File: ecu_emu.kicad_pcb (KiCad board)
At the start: 2 copper layers, 51.3 x 16.5 mm, 29 parts, among them J1 Conn_02x06_Odd_Even, J2 Conn_01x04_Male, Q1 IRF7201PBF, U1 LD1117S33TR_SOT223, U2 STM32F105RBTx, U3 FAN73711, U4 E-L9637D, Y1 Crystal KX-9A

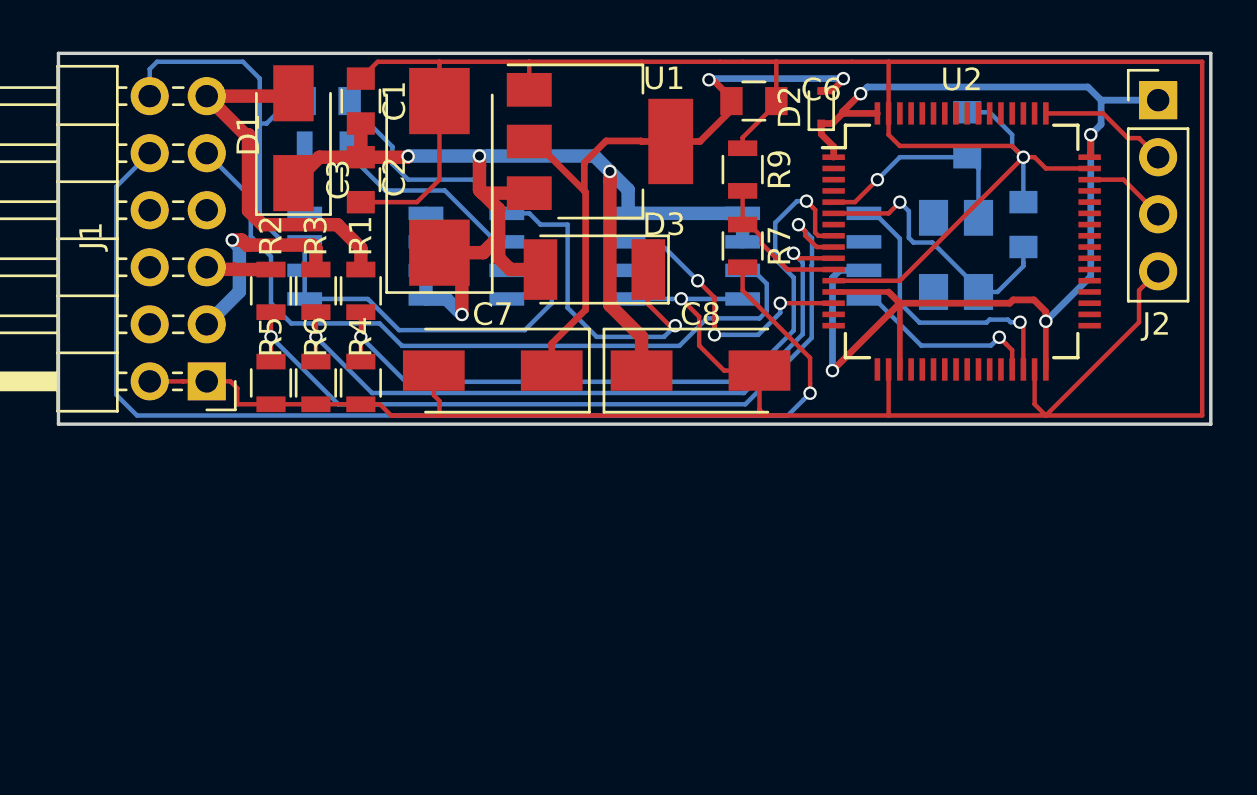
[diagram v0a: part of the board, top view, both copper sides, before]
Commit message: scheme: change solenoid driver, add capasitors to stm power supply, fix crystal package
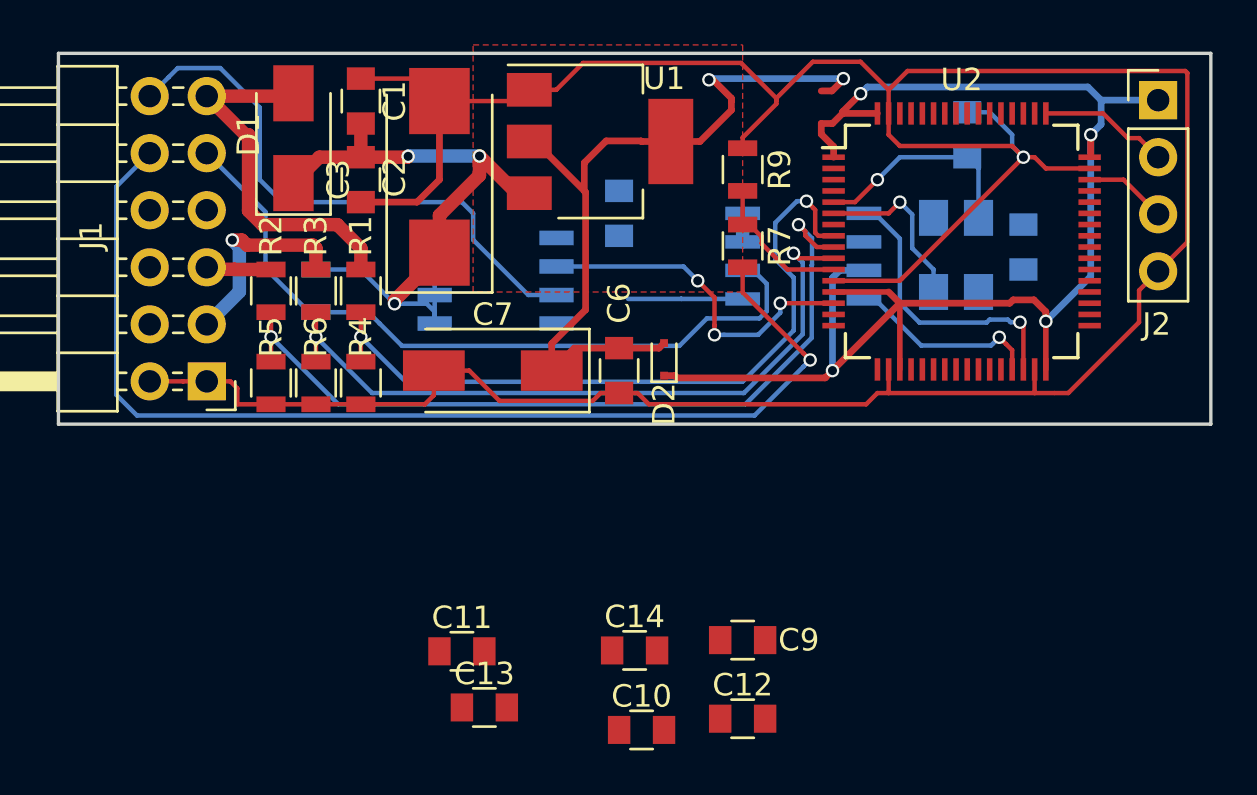
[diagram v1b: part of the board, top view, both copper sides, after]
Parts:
- removed D3: SM4007, Diodes_SMD:D_MELF
- removed Q1: IRF7201PBF, Housings_SOIC:SOIC-8_3.9x4.9mm_Pitch1.27mm
- added C10: 100nF, Capacitors_SMD:C_0805, F.Cu at (123.5, 109.5)
- added C11: 100nF, Capacitors_SMD:C_0805, F.Cu at (115.5, 106.0)
- added C12: 100nF, Capacitors_SMD:C_0805, F.Cu at (128.0, 109.0)
- added C13: 100nF, Capacitors_SMD:C_0805, F.Cu at (116.5, 108.5)
- added C14: 100nF, Capacitors_SMD:C_0805, F.Cu at (123.2, 106.0)
- C8: value 47uF x 16V -> 1nF; footprint Capacitors_Tantalum_SMD:CP_Tantalum_Case-C_EIA-6032-28_Wave -> Capacitors_SMD:C_0805; moved to B.Cu
- C9: value 1000 pF -> 4.7uF; moved to F.Cu
- R8: value 65 -> 1k
- U3: value FAN73711 -> BSP742R; footprint Housings_SOIC:SOIC-8_3.9x4.9mm_Pitch1.27mm -> zulljon:SOIC127P600X175-8N
- moved C9 30.3 mm to (128.0, 105.5)
- moved C6 13.4 mm to (122.5, 93.5), turned to 270 degrees
- moved D2 13.2 mm to (124.5, 93.0)
- moved C8 7.88 mm to (122.5, 86.5), turned to 90 degrees
- moved R8 6.47 mm to (109.0, 90.0), turned to 90 degrees
- moved U3 3.38 mm to (117.0, 89.5)
- moved C5 1.00 mm to (140.5, 88.0)
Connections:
- net /stm2K-BUS_UART_RX renamed /stm2Kbus_UART_RX
- net /stm2K-BUS_UART_TX renamed /stm2Kbus_UART_TX
- C1 pad 1: /K-BUS_Vbatt -> /Kbus_Vbatt
- C2 pad 1: /K-BUS_Vbatt -> /Kbus_Vbatt
- C3 pad 1: /K-BUS_Vbatt -> /Kbus_Vbatt
- C8 pad 1: /K-BUS_Vbatt -> /ECU_Kbus
- C9 pad 1: Net-(C9-Pad1) -> /+3V3_STM
- C9 pad 2: /ECU_solenoid -> GND
- D1 pad 1: /K-BUS_Vbatt -> /Kbus_Vbatt
- J1 pad 9: /ECU_K-BUS -> /ECU_Kbus
- R8 pad 1: Net-(Q1-Pad4) -> /ECU_Kbus
- R8 pad 2: Net-(R8-Pad2) -> /Kbus_Vbatt
- U1 pad 3: /K-BUS_Vbatt -> /Kbus_Vbatt
- U3 pad 1: /K-BUS_Vbatt -> GND
- U3 pad 3: (no net) -> /ECU_solenoid
- U3 pad 4: GND -> (no net)
- U3 pad 5: (no net) -> /Kbus_Vbatt
- U3 pad 6: /ECU_solenoid -> /Kbus_Vbatt
- U3 pad 7: Net-(R8-Pad2) -> /Kbus_Vbatt
- U3 pad 8: Net-(C9-Pad1) -> /Kbus_Vbatt
- U4 pad 6: /ECU_K-BUS -> /ECU_Kbus
- U4 pad 7: /K-BUS_Vbatt -> /Kbus_Vbatt
- U4 pad 8: /K-BUS_Vbatt -> /Kbus_Vbatt
- Y1 pad 2: Net-(C5-Pad1) -> GND
- Y1 pad 3: (no net) -> Net-(C5-Pad1)
- Y1 pad 4: (no net) -> GND
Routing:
- net /K-BUS_Vbatt: track 55.3 -> 0.00 mm, vias 4 -> 0
- net /ECU_K-BUS: track 33.9 -> 0.00 mm
- net /ECU_Kbus: track 0.00 -> 33.6 mm
- net /Kbus_Vbatt: track 0.00 -> 33.0 mm, vias 0 -> 3
- net GND: track 173.2 -> 144.2 mm, vias 2 -> 1
- net Net-(C9-Pad1): track 24.9 -> 0.00 mm, vias 1 -> 0
- net /ECU_solenoid: track 35.1 -> 25.4 mm
- net Net-(R8-Pad2): track 9.04 -> 0.00 mm
- net /+3V3_STM: track 56.5 -> 64.2 mm
- net /+3V3: track 29.9 -> 35.4 mm
- net Net-(C5-Pad1): track 12.4 -> 7.78 mm
- net Net-(Q1-Pad4): track 3.00 -> 0.00 mm
- net /solenoid_driver: track 12.7 -> 15.4 mm
- net /ECU_HALL_sensor+: track 49.9 -> 49.0 mm
- added copper zone on F.Cu, net /+3V3

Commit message: pcb: swd conn to socket strip, applied sch changes from 059fb19
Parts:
- C10, C11, C12, C13, C14, C9, R7, R9: moved to B.Cu
- J2: footprint Pin_Headers:Pin_Header_Straight_1x04_Pitch2.54mm -> Socket_Strips:Socket_Strip_Angled_1x04_Pitch2.54mm
- U3: footprint zulljon:SOIC127P600X175-8N -> Housings_SOIC:SOIC-8_3.9x4.9mm_Pitch1.27mm
- moved C13 36.1 mm to (140.5, 81.5), turned to 180 degrees
- moved C11 28.9 mm to (140.5, 91.5), turned to 180 degrees
- moved C10 27.8 mm to (140.5, 87.5), turned to 180 degrees
- moved C12 26.6 mm to (140.5, 85.5), turned to 180 degrees
- moved C9 25.3 mm to (140.5, 83.5)
- moved C14 23.9 mm to (140.5, 89.5), turned to 180 degrees
- moved C8 13.5 mm to (109.0, 86.0), turned to 270 degrees
- moved J2 9.98 mm to (146.5, 91.4), turned to 180 degrees
- moved U4 6.18 mm to (124.6, 89.5)
- moved R7 6.03 mm to (129.0, 82.0)
- moved C5 4.74 mm to (136.0, 89.5), turned to 0 degrees
- moved R9 4.33 mm to (131.5, 82.0)
- moved Y1 3.22 mm to (136.0, 85.5)
- moved C4 2.50 mm to (136.0, 81.5), turned to 0 degrees
- moved U3 1.26 mm to (115.7, 89.5)
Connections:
- J1 pad 4: (no net) -> /ECU_P/N
- J1 pad 6: (no net) -> Net-(J1-Pad6)
- J1 pad 7: (no net) -> Net-(J1-Pad7)
- J1 pad 8: (no net) -> /Transmission_control_module
- J2 pad 1: /+3V3_STM -> GND
- J2 pad 4: GND -> /+3V3_STM
- U2 pad 15: (no net) -> Net-(U2-Pad15)
- U2 pad 16: (no net) -> Net-(U2-Pad16)
- U2 pad 17: (no net) -> Net-(U2-Pad17)
- U2 pad 2: (no net) -> Net-(U2-Pad2)
- U2 pad 20: (no net) -> Net-(U2-Pad20)
- U2 pad 21: (no net) -> Net-(U2-Pad21)
- U2 pad 22: (no net) -> Net-(U2-Pad22)
- U2 pad 23: (no net) -> Net-(U2-Pad23)
- U2 pad 24: (no net) -> Net-(U2-Pad24)
- U2 pad 25: (no net) -> Net-(U2-Pad25)
- U2 pad 26: (no net) -> Net-(U2-Pad26)
- U2 pad 27: (no net) -> Net-(U2-Pad27)
- U2 pad 28: (no net) -> Net-(U2-Pad28)
- U2 pad 3: (no net) -> Net-(U2-Pad3)
- U2 pad 33: (no net) -> Net-(U2-Pad33)
- U2 pad 34: (no net) -> Net-(U2-Pad34)
- U2 pad 35: (no net) -> Net-(U2-Pad35)
- U2 pad 36: (no net) -> Net-(U2-Pad36)
- U2 pad 37: (no net) -> Net-(U2-Pad37)
- U2 pad 38: (no net) -> Net-(U2-Pad38)
- U2 pad 39: (no net) -> Net-(U2-Pad39)
- U2 pad 4: (no net) -> Net-(U2-Pad4)
- U2 pad 40: (no net) -> Net-(U2-Pad40)
- U2 pad 41: (no net) -> Net-(U2-Pad41)
- U2 pad 42: (no net) -> Net-(U2-Pad42)
- U2 pad 43: (no net) -> Net-(U2-Pad43)
- U2 pad 44: (no net) -> Net-(U2-Pad44)
- U2 pad 45: (no net) -> Net-(U2-Pad45)
- U2 pad 50: (no net) -> Net-(U2-Pad50)
- U2 pad 51: (no net) -> Net-(U2-Pad51)
- U2 pad 52: (no net) -> Net-(U2-Pad52)
- U2 pad 53: (no net) -> Net-(U2-Pad53)
- U2 pad 54: (no net) -> Net-(U2-Pad54)
- U2 pad 55: (no net) -> Net-(U2-Pad55)
- U2 pad 56: (no net) -> Net-(U2-Pad56)
- U2 pad 57: (no net) -> Net-(U2-Pad57)
- U2 pad 58: (no net) -> Net-(U2-Pad58)
- U2 pad 59: (no net) -> Net-(U2-Pad59)
- U2 pad 60: (no net) -> Net-(U2-Pad60)
- U2 pad 61: (no net) -> Net-(U2-Pad61)
- U2 pad 62: (no net) -> Net-(U2-Pad62)
- U2 pad 7: (no net) -> Net-(U2-Pad7)
- U3 pad 4: (no net) -> Net-(U3-Pad4)
- U4 pad 2: (no net) -> Net-(U4-Pad2)
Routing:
- net GND: track 144.2 -> 176.8 mm, vias 1 -> 6
- net /stm2Kbus_UART_TX: track 8.71 -> 24.2 mm
- net /Kbus_Vbatt: track 33.0 -> 45.3 mm
- net /+3V3: track 35.4 -> 23.6 mm, vias 2 -> 0
- net /stm2Kbus_UART_RX: track 12.9 -> 22.4 mm
- net /+3V3_STM: track 64.2 -> 73.0 mm, vias 4 -> 5
- net /ECU_HALL_sensor+: track 49.0 -> 56.2 mm, vias 1 -> 2
- net Net-(R7-Pad1): track 6.55 -> 12.3 mm, vias 0 -> 1
- net /ECU_Kbus: track 33.6 -> 28.5 mm
- net Net-(J2-Pad2): track 5.81 -> 10.5 mm
- net /ECU_solenoid: track 25.4 -> 22.7 mm
- net /ADC_IGN: track 36.1 -> 37.9 mm
- net /ADC_AUX: track 31.6 -> 33.4 mm
- net /ADC_Vbatt: track 32.6 -> 34.1 mm
- net /ECU_AUX: track 9.30 -> 8.29 mm
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- added copper zone on B.Cu, net /Kbus_Vbatt
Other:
- rule trace_min: 0.2 -> 0.1

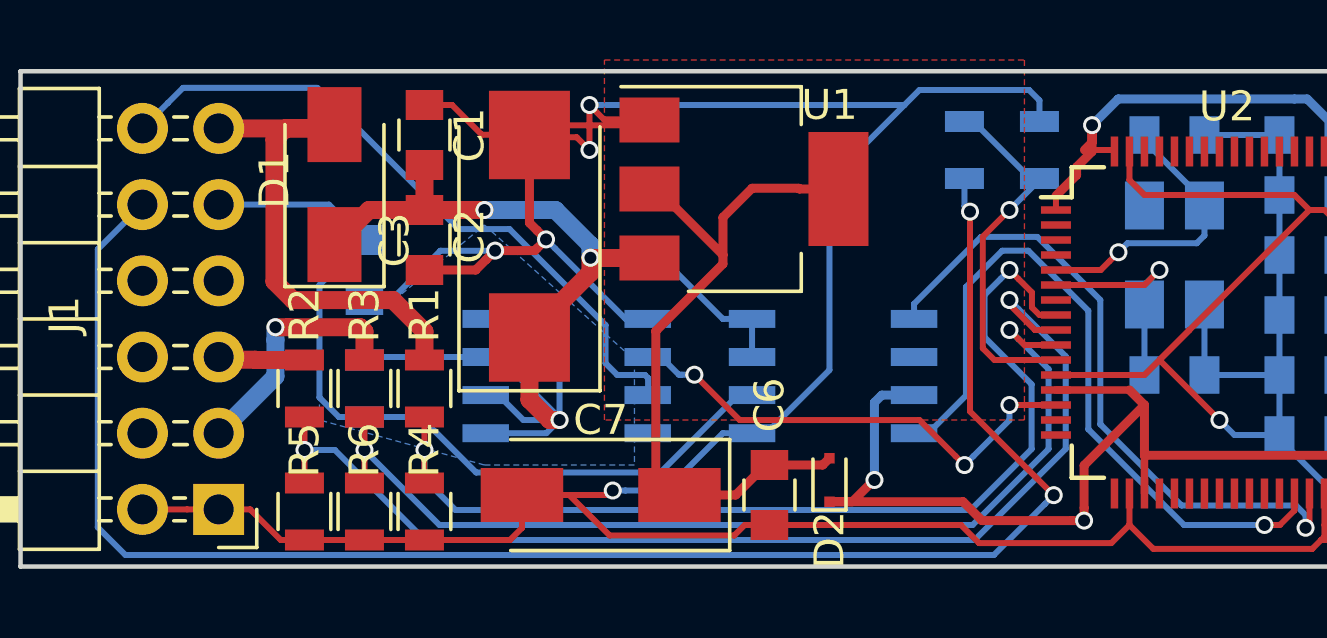
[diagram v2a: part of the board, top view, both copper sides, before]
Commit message: pcb: add additional vias and zones to linear stabilazer on bottom side
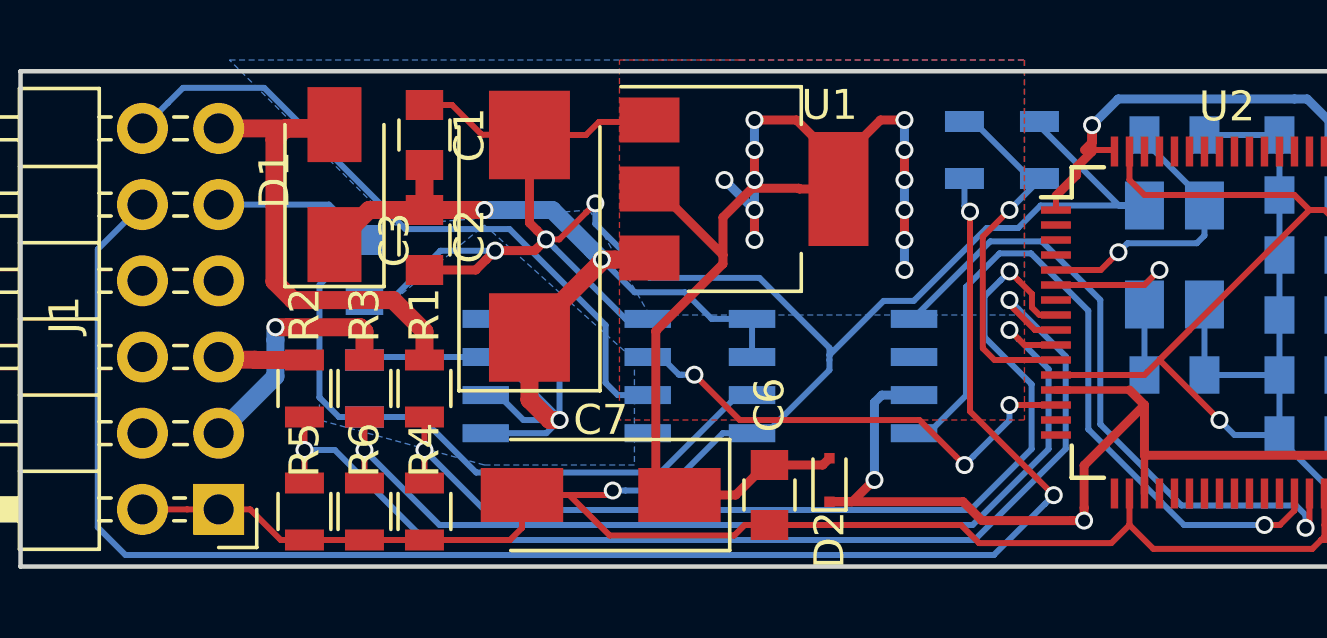
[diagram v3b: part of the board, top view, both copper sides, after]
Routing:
- net /+3V3: track 23.6 -> 42.1 mm, vias 0 -> 12
- net GND: track 176.8 -> 175.9 mm, vias 6 -> 5
- net /ADC_Vbatt: track 34.1 -> 33.4 mm
- net /Kbus_Vbatt: track 45.3 -> 44.8 mm
- added copper zone on B.Cu, net /+3V3

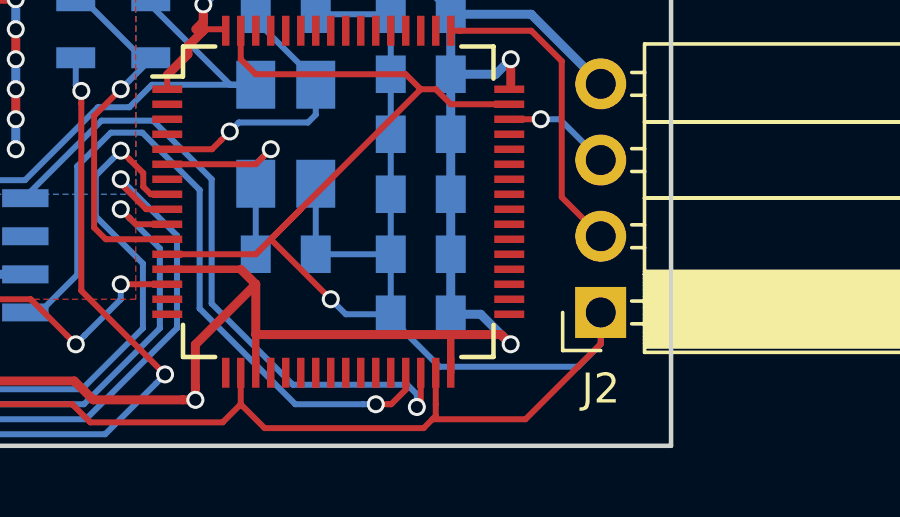
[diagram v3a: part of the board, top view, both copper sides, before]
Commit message: sch&pcb: add one LED and refresh readme image
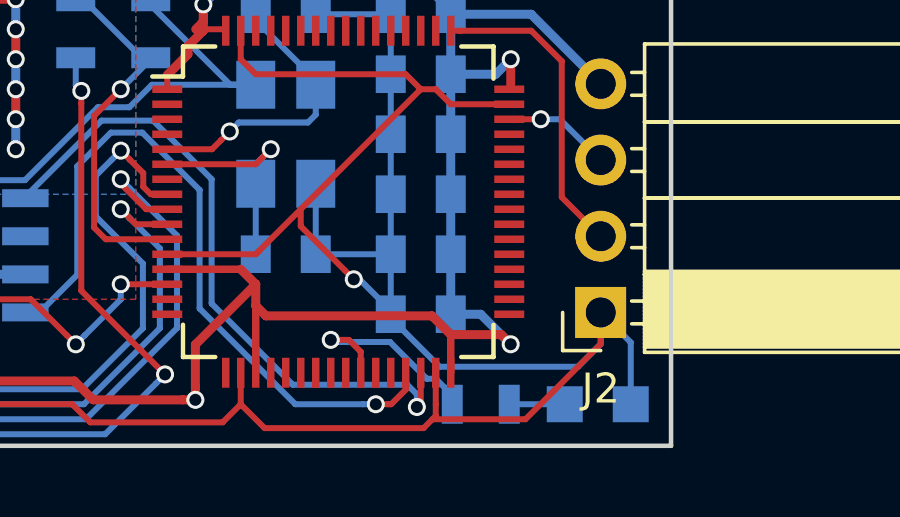
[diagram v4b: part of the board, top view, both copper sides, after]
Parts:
- added D3: LED, LEDs:LED_0805, B.Cu at (146.4, 94.5)
- added R10: 1k, Resistors_SMD:R_0805, B.Cu at (142.5, 94.5)
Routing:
- net Net-(R10-Pad2): track 0.00 -> 6.98 mm, vias 0 -> 1
- net GND: track 175.9 -> 177.7 mm
- net Net-(D3-Pad2): track 0.00 -> 1.85 mm
- net /+3V3_STM: track 73.0 -> 72.4 mm

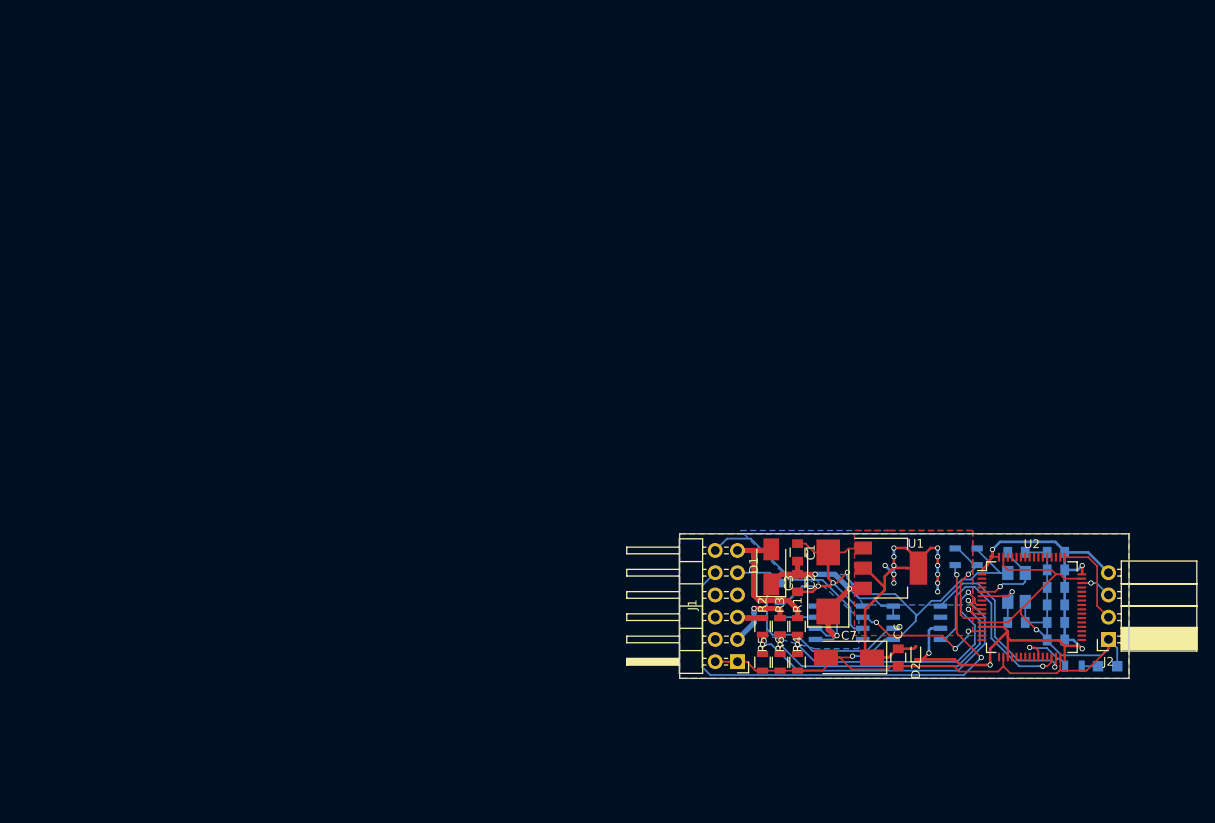
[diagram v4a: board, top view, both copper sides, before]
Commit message: generate gerber files & add .sh to zip them
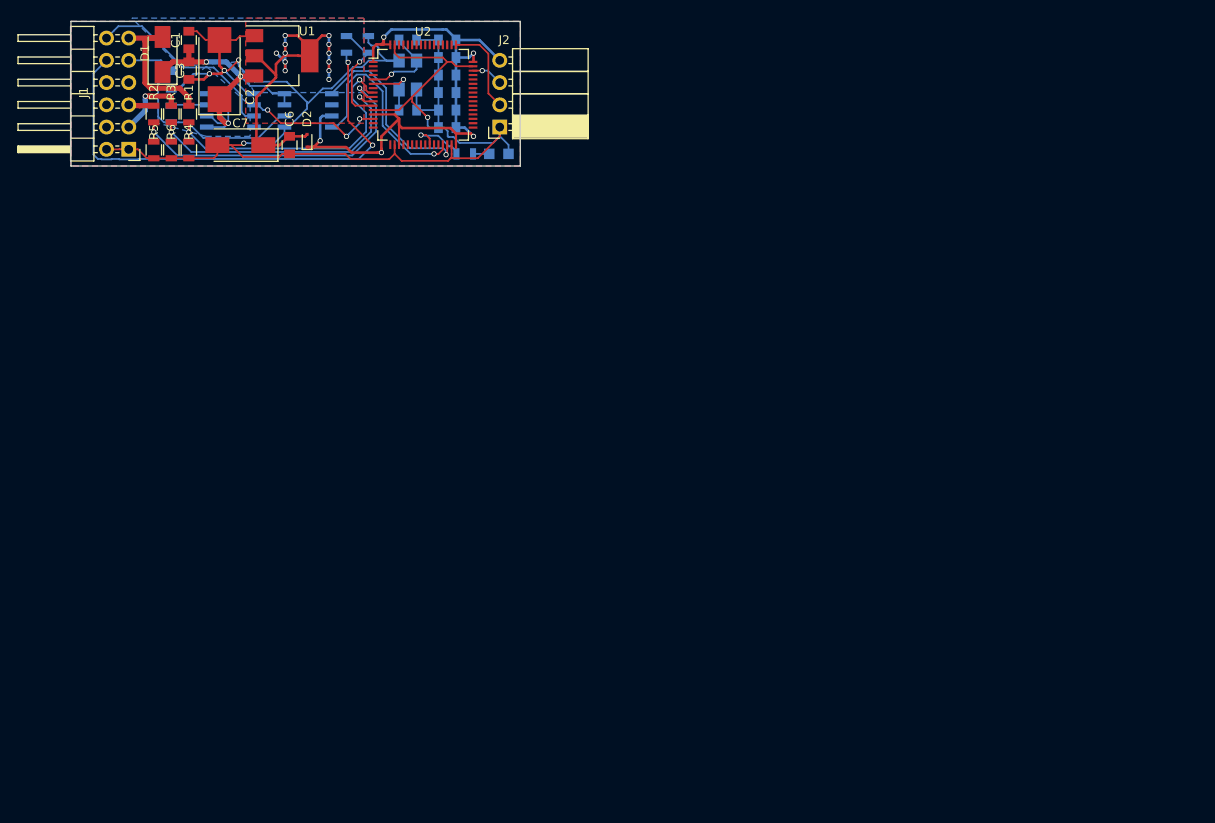
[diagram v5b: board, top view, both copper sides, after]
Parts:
- moved C1 90.8 mm to (41.5, 23.0)
- moved C10 90.8 mm to (71.0, 29.0)
- moved C11 90.8 mm to (71.0, 33.0)
- moved C12 90.8 mm to (71.0, 27.0)
- moved C13 90.8 mm to (71.0, 23.0)
- moved C14 90.8 mm to (71.0, 31.0)
- moved C2 90.8 mm to (45.0, 26.4)
- moved C3 90.8 mm to (41.5, 26.5)
- moved C4 90.8 mm to (66.5, 23.0)
- moved C5 90.8 mm to (66.5, 31.0)
- moved C6 90.8 mm to (53.0, 35.0)
- moved C7 90.8 mm to (47.4, 35.0)
- moved C8 90.8 mm to (39.5, 27.5)
- moved C9 90.8 mm to (71.0, 25.0)
- moved D1 90.8 mm to (38.5, 24.7)
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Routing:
- net GND: track 177.7 -> 179.6 mm
